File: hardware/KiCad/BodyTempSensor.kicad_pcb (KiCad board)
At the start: 4 copper layers, 78.9 x 39 mm, 83 parts, among them IC3 TMP117MAIDRVT, IC4 TMP117MAIDRVT, IC5 TMP117MAIDRVT, IC6 TMP117MAIDRVT, IC7 NRF54L15-QFAA-R, J1 USB_C_Receptacle_USB2.0, J2 Conn_02x02_Odd_Even, J3 BAT, J4 Conn_02x02_Odd_Even, J5 Conn_02x02_Odd_Even, J6 Conn_02x05_Odd_Even, J7 Conn_02x02_Odd_Even, Q1 NMOS, Q2 NMOS, U3 MCP73833-xxx-UN, U4 TLV62568DBVR, U5 MCP6001-OT, Y1 32MHz

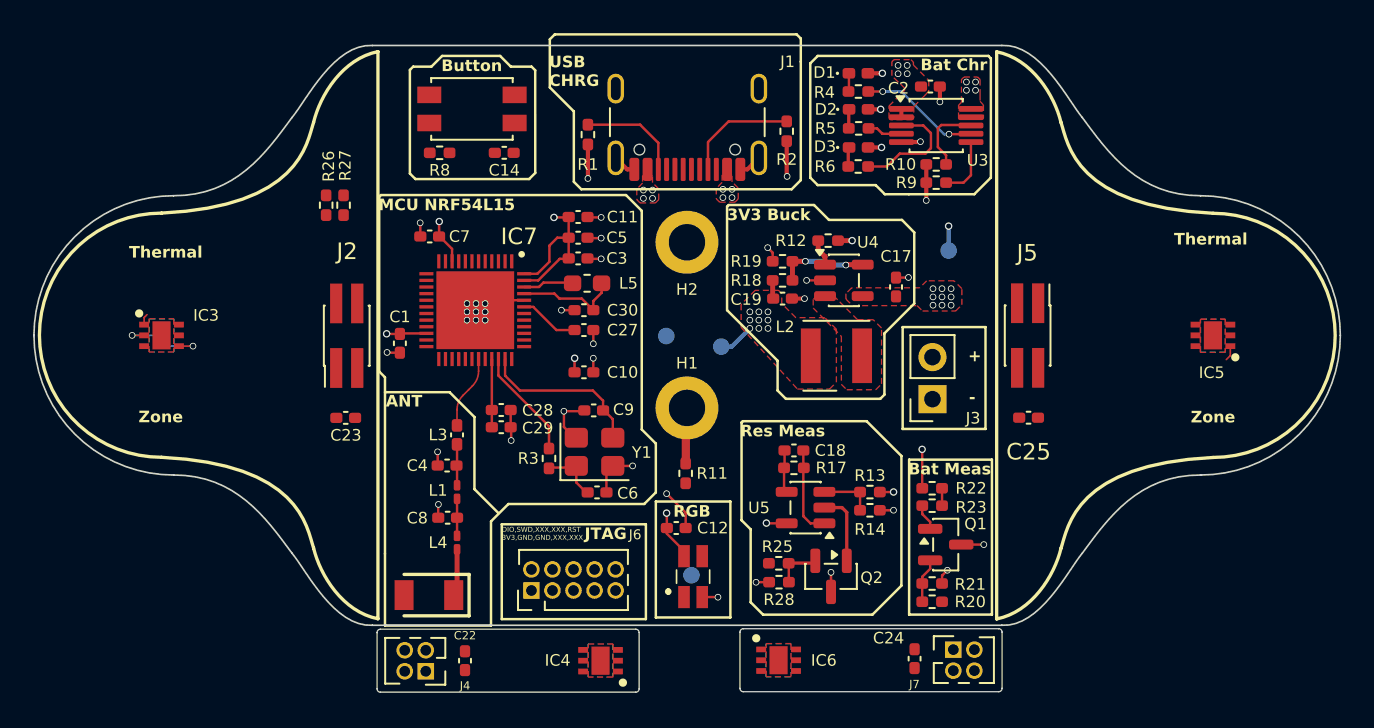
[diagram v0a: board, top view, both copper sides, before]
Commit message: Add new STEP files for KiCad and finalize the lay-out.
- Created new STEP file: Step3DBoard.step (5.1 MB)
- Created new STEP file: Unnamed1-Step3DBoard 1.step (7.8 MB)
- Added Excel data file: ~$BodyTempSens_Data.xlsx with initial data
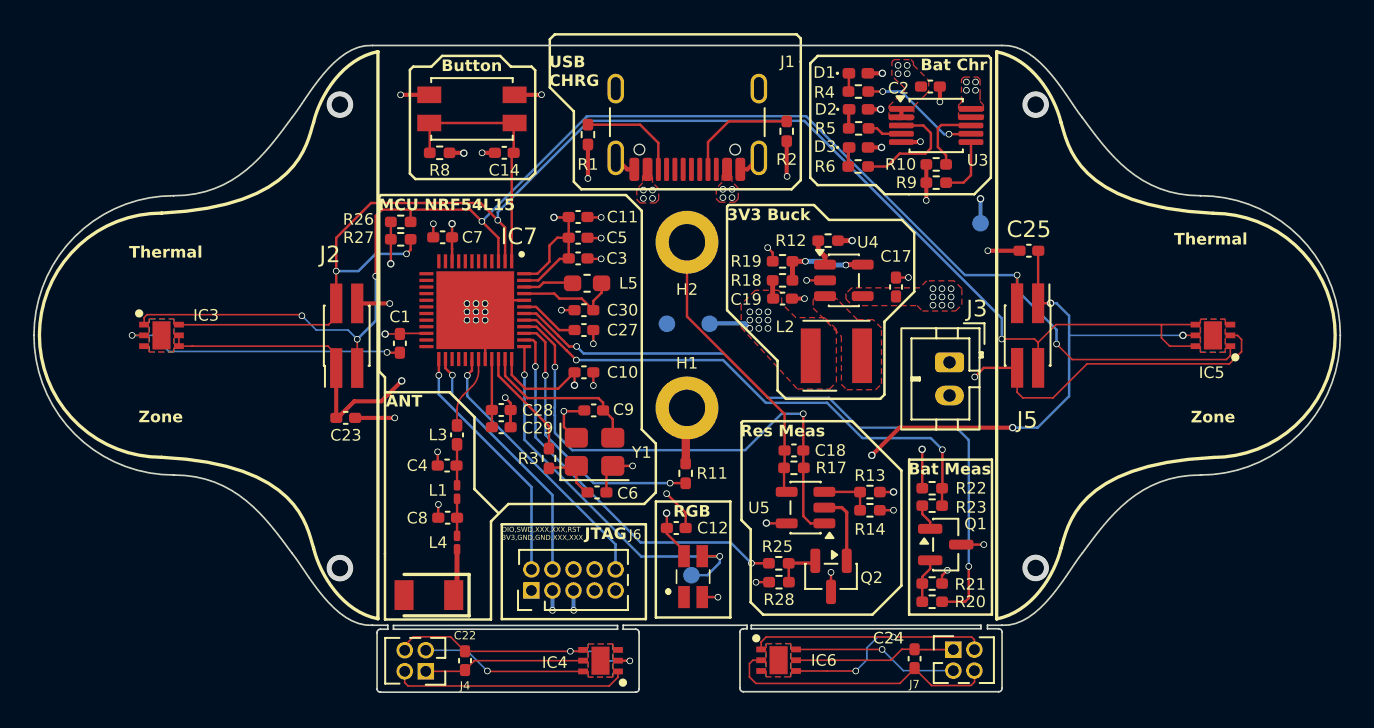
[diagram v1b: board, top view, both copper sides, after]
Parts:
- J3: footprint Connector_PinSocket_2.54mm:PinSocket_1x02_P2.54mm_Vertical -> Connector_JST:JST_PH_B2B-PH-K_1x02_P2.00mm_Vertical
- moved C25 10.1 mm to (205.5, 94.4), turned to 180 degrees
- moved R26 4.61 mm to (167.6, 92.6), turned to 0 degrees
- moved R27 4.02 mm to (167.6, 93.7), turned to 0 degrees
- moved TP3 2.54 mm to (202.6, 92.7)
- moved J3 2.45 mm to (200.7, 101.1), turned to -90 degrees
- moved TP4 1.55 mm to (186.2, 98.8)
- moved C7 0.78 mm to (170.1, 93.5)
- moved TP1 0.74 mm to (183.7, 98.8)
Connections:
- IC7 pad 1: unconnected-(IC7I/O-P1.00/XL1-Pad1) -> /IO_BTN_ACT
- IC7 pad 2: unconnected-(IC7I/O-P1.01/XL2-Pad2) -> /P0.17/SDA
- IC7 pad 3: unconnected-(IC7I/O-P1.02/NFC1-Pad3) -> /P0.19/SCL
- IC7 pad 37: unconnected-(IC7I/O-P1.09/TAMPC-Pad37) -> /IO_RGB
- IC7 pad 38: unconnected-(IC7I/O-P1.10/TAMPC-Pad38) -> /IO_IMP_PWR
- IC7 pad 39: unconnected-(IC7I/O-P1.11/AIN4-Pad39) -> /IO_IMP_IN
- IC7 pad 40: unconnected-(IC7I/O-P1.12/AIN5-Pad40) -> /IO_IMP_OUT
- IC7 pad 41: unconnected-(IC7I/O-P1.13/AIN6-Pad41) -> /IO_BAT_MEAS
- IC7 pad 42: unconnected-(IC7I/O-P1.14/AIN7-Pad42) -> /IO_BAT_MEAS_ON
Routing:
- net /P0.19/SCL: track 1.58 -> 126.9 mm, vias 0 -> 8
- net /P0.17/SDA: track 0.00 -> 110.1 mm, vias 0 -> 6
- net Earth: track 48.1 -> 127.9 mm, vias 40 -> 50
- net +3V3: track 25.2 -> 104.1 mm, vias 16 -> 23
- net /IO_BAT_MEAS_ON: track 0.00 -> 41.3 mm, vias 0 -> 2
- net /IO_BAT_MEAS: track 1.05 -> 31.9 mm, vias 0 -> 2
- net /IO_IMP_OUT: track 5.42 -> 31.6 mm, vias 0 -> 2
- net /IO_RGB: track 0.00 -> 23.8 mm, vias 0 -> 2
- net /IO_IMP_PWR: track 0.00 -> 23.7 mm, vias 0 -> 2
- net /IO_IMP_IN: track 0.00 -> 16.8 mm, vias 0 -> 2
- net /nRF_RESET: track 0.00 -> 16.5 mm, vias 0 -> 1
- net /nRF_SWD_CLK: track 0.00 -> 15.4 mm, vias 0 -> 1
- net /IO_BTN_ACT: track 0.00 -> 15.4 mm
- net /nRF_SWD_DIO: track 0.00 -> 15.0 mm, vias 0 -> 1
- net Net-(U5--): track 2.58 -> 17.6 mm
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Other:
- outline, holes or cut-outs redrawn
- board text removed: "+"
- board text removed: "-"

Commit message: Feat: Finalized PCB and added V1 and V2 of the Casing
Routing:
- net +3V3: track 104.1 -> 105.1 mm, vias 23 -> 24
- net /P0.17/SDA: track 110.1 -> 109.4 mm
